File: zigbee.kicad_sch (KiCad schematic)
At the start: 59 parts, among them J201 Conn_Coaxial, J203 TC2050, U201 SKY13317-373, U202 CC2652P1FRGZR, U203 CC2652P1FRGZR, U204 CC2652PSIP, X201 32.768kHz, X202 48MHz

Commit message: Fixed SoC power circuitry
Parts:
- removed C201, C204, C206, C210: 1.5p, symbol Device:C
- removed C202, C221, C222, C223, C224, C225, C226: 0.1u, symbol Device:C
- removed C203, C219, C220: 22u, symbol Device:C
- removed C205: 0.5p, symbol Device:C
- removed C207, C211, C212, C216, C229: 12p, symbol Device:C
- removed C208: 15p, symbol Device:C
- removed C209: 1u, symbol Device:C
- removed C213, C214: 7.5p, symbol Device:C
- removed C215: 10n, symbol Device:C
- removed C217, C218, C227, C228: 1p, symbol Device:C
- removed C230: 470p, symbol Device:C
- removed D201: D_TVS, symbol Device:D_TVS
- removed J201: Conn_Coaxial, symbol Connector:Conn_Coaxial
- removed L201: 6.8u, symbol Device:L
- removed L202: 6.8n, symbol Device:L
- removed L203, L204: 2.4n, symbol Device:L
- removed L205: 3.3n, symbol Device:L
- removed L206: 2.7n, symbol Device:L
- removed L207: 20n, symbol Device:L
- removed L208, L209: 3.7n, symbol Device:L
- removed L210, L211: 3.4n, symbol Device:L
- removed R201: 100k, symbol Device:R
- removed R202, R207, R208: 0R, symbol Device:R
- removed U201: SKY13317-373, symbol SoftServicesSymbolLibrary:SKY13317-373
- removed U202, U203: CC2652P1FRGZR, symbol SoftServicesSymbolLibrary:CC2652P1FRGZR
- removed X201: 32.768kHz, symbol Device:Crystal
- removed X202: 48MHz, symbol Device:Crystal_GND24
- added C2001: 0.1u, symbol Device:C
- added C2002: 15p, symbol Device:C
- added J2002: Conn_Coaxial, symbol Connector:Conn_Coaxial
- added R2001: R, symbol Device:R
- U2001: renamed from U204; footprint (none) -> CC2652PSIP:CC2652PSIP
- renumbered FB201 to FB2001, J203 to J2001, R203 to R2002, R204 to R2003, R205 to R2004, R206 to R2005
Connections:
- net CC2652_LED1: now also U2001.24 (DIO6)
- net CC2652_LED2: now also U2001.25 (DIO7)
- net CC2652_RESET_N: now also U2001.4 (nRESET), C2001.1
- net CC2652_TCK: now also U2001.35 (TCK)
- net CC2652_TDI: now also U2001.37 (DIO17)
- net CC2652_TDO: now also U2001.36 (DIO16)
- net CC2652_TMS: now also U2001.34 (TMS)
- net CC2652_UART6_CTSn: now also R2005.2; no longer R2004.2
- net CC2652_UART6_RTSn: now also R2004.2; no longer R2005.2
- net CC2652_UART6_RXD: now also R2002.1; no longer R2003.1
- net CC2652_UART6_TXD: now also R2003.1; no longer R2002.1
- net GND: now also J2001.9, U2001.10 (GND), U2001.11 (GND), U2001.12 (GND), U2001.13 (GND), U2001.16 (GND), U2001.17 (GND), U2001.19 (GND), U2001.49 (GND), U2001.5 (GND), U2001.50 (GND), U2001.51 (GND), U2001.52 (GND), U2001.53 (GND), U2001.54 (GND), U2001.55 (GND), U2001.56 (GND), U2001.57 (GND), U2001.58 (GND), U2001.59 (GND), U2001.60 (GND), U2001.61 (GND), U2001.62 (GND), U2001.63 (GND), U2001.64 (GND), U2001.65 (GND), U2001.66 (GND), U2001.67 (GND), U2001.68 (GND), U2001.69 (GND), U2001.70 (GND), U2001.71 (GND), U2001.72 (GND), U2001.73 (GND), U2001.9 (GND), C2001.2, J2002.2 (Ext)
- net VDD3V3_CC: now also U2001.46 (VDDS), U2001.47 (VDDS_PU), R2001.2
- net VDD_3V3: now also R2001.1
- net at R2002.2: now also U2001.30 (DIO12)
- net at R2003.2: now also U2001.31 (DIO13)
- net at R2004.1: now also U2001.39 (DIO18)
- net at R2005.1: now also U2001.40 (DIO19)
- net at U2001.18 (RF): now also C2002.1
- new net: C2002.2, J2002.1 (In)
- no-connect marks 18 -> 2
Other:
- note added: "CC2652PSIP Zigbee Network"
- note removed: "CC2652P I/O Interface"
- note removed: "CC2652P Zigbee Network"
- note removed: "Decoupling Capacitors"
- note removed: "Need to configure GPIO for antenna to be connected to a path"
- moved on the sheet: FB2001, J2001, R2002, R2003, R2004, R2005, U2001

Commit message: Finished SoC schematic
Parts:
- removed R2001: R, symbol Device:R
- added D2001, D2002, D2003: D, symbol Device:D
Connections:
- net CC2652_RESET_N: now also D2001.2 (A), D2002.2 (A), D2003.2 (A)
- net CC2652_BOOT: now reaches U2001.33 (DIO15)
- new net CC2652_RSTn: D2001.1 (K)
- new net PORz_OUT: D2002.1 (K)
- new net RESETSTATz: D2003.1 (K)
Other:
- note added: "RB520S30T1G"

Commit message: Fixed ERC errors and warnings (zero errors and zero warnings)
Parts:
- renumbered R2002 to R2001, R2003 to R2002, R2004 to R2003, R2005 to R2004
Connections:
- no-connect marks 2 -> 25
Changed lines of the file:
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@@
+	)
+	(junction
+		(at 215.9 78.74)
+		(diameter 0)
+		(color 0 0 0 0)
 	)
 	(junction
@@
 	)
 	(no_connect
+		(at 133.35 129.54)
+	)
+	(no_connect
+		(at 133.35 111.76)
+	)
+	(no_connect
+		(at 133.35 167.64)
+	)
+	(no_connect
+		(at 133.35 172.72)
+	)
+	(no_connect
+		(at 133.35 109.22)
+	)
+	(no_connect
+		(at 133.35 175.26)
+	)
+	(no_connect
+		(at 133.35 182.88)
+	)
+	(no_connect
 		(at 300.99 95.25)
+	)
+	(no_connect
+		(at 133.35 116.84)
+	)
+	(no_connect
+		(at 133.35 132.08)
 	)
 	(no_connect
 		(at 133.35 96.52)
 	)
+	(no_connect
+		(at 133.35 157.48)
+	)
+	(no_connect
+		(at 133.35 165.1)
+	)
+	(no_connect
+		(at 133.35 160.02)
+	)
+	(no_connect
+		(at 133.35 127)
+	)
+	(no_connect
+		(at 133.35 185.42)
+	)
+	(no_connect
+		(at 133.35 177.8)
+	)
+	(no_connect
+		(at 133.35 162.56)
+	)
+	(no_connect
+		(at 133.35 180.34)
+	)
+	(no_connect
+		(at 133.35 142.24)
+	)
+	(no_connect
+		(at 133.35 134.62)
+	)
+	(no_connect
+		(at 133.35 114.3)
+	)
+	(no_connect
+		(at 133.35 106.68)
+	)
+	(no_connect
+		(at 133.35 170.18)
+	)
+	(no_connect
+		(at 133.35 119.38)
+	)
 	(wire
 		(pts
@@
 	(wire
 		(pts
-			(xy 217.17 73.66) (xy 217.17 78.74)
+			(xy 222.25 73.66) (xy 222.25 78.74)
 		)
 		(stroke
@@
 	(wire
 		(pts
-			(xy 210.82 78.74) (xy 217.17 78.74)
+			(xy 210.82 78.74) (xy 215.9 78.74)
 		)
 		(stroke
@@
 		(pts
 			(xy 100.33 114.3) (xy 100.33 116.84)
+		)
+		(stroke
+			(width 0)
+			(type default)
+		)
+	)
+	(wire
+		(pts
+			(xy 215.9 78.74) (xy 222.25 78.74)
 		)
 		(stroke
@@
 	)
 	(symbol
+		(lib_id "power:PWR_FLAG")
+		(at 215.9 78.74 0)
+		(unit 1)
+		(exclude_from_sim no)
+		(in_bom yes)
+		(on_board yes)
+		(dnp no)
+		(property "Reference" "#FLG04038"
+			(at 215.9 76.835 0)
+			(effects
+				(font
+					(size 1.27 1.27)
+				)
+				(hide yes)
+			)
+		)
+		(property "Value" "PWR_FLAG"
+			(at 215.9 74.422 0)
+			(effects
+				(font
+					(size 1.27 1.27)
+				)
+			)
+		)
+		(property "Footprint" ""
+			(at 215.9 78.74 0)
+			(effects
+				(font
+					(size 1.27 1.27)
+				)
+				(hide yes)
+			)
+		)
+		(property "Datasheet" "~"
+			(at 215.9 78.74 0)
+			(effects
+				(font
+					(size 1.27 1.27)
+				)
+				(hide yes)
+			)
+		)
+		(property "Description" "Special symbol for telling ERC where power comes from"
+			(at 215.9 78.74 0)
+			(effects
+				(font
+					(size 1.27 1.27)
+				)
+				(hide yes)
+			)
+		)
+		(pin "1"
+		)
+		(instances
+			(project "Leonhart"
+				(path "/b43b7bca-e50d-42ec-8ff0-e0016dfefe0a/4037e4ca-7763-453b-96d1-7d8342daaa99"
+					(reference "#FLG04038")
+					(unit 1)
+				)
+			)
+		)
+	)
+	(symbol
 		(lib_id "Device:C")
 		(at 148.59 101.6 90)
@@
 	(symbol
 		(lib_id "power:VDD")
-		(at 217.17 73.66 0)
+		(at 222.25 73.66 0)
 		(unit 1)
 		(exclude_from_sim no)
@@
 		(dnp no)
 		(property "Reference" "#PWR02002"
-			(at 217.17 77.47 0)
+			(at 222.25 77.47 0)
 			(effects
 				(font
@@
 		)
 		(property "Value" "VDD3V3_CC"
-			(at 212.852 68.58 0)
+			(at 217.932 68.58 0)
 			(effects
 				(font
@@
 		)
 		(property "Footprint" ""
-			(at 217.17 73.66 0)
+			(at 222.25 73.66 0)
 			(effects
 				(font
@@
 		)
 		(property "Datasheet" ""
-			(at 217.17 73.66 0)
+			(at 222.25 73.66 0)
 			(effects
 				(font
@@
 		)
 		(property "Description" "Power symbol creates a global label with name \"VDD\""
-			(at 217.17 73.66 0)
+			(at 222.25 73.66 0)
 			(effects
 				(font
@@
 		(on_board yes)
 		(dnp no)
-		(property "Reference" "R2005"
+		(property "Reference" "R2004"
 			(at 157.48 157.734 90)
 			(effects
@@
 			(project "Leonhart"
 				(path "/b43b7bca-e50d-42ec-8ff0-e0016dfefe0a/4037e4ca-7763-453b-96d1-7d8342daaa99"
-					(reference "R2005")
+					(reference "R2004")
 					(unit 1)
 				)
@@
 		(on_board yes)
 		(dnp no)
-		(property "Reference" "R2003"
+		(property "Reference" "R2002"
 			(at 157.48 142.494 90)
 			(effects
@@
 			(project "Leonhart"
 				(path "/b43b7bca-e50d-42ec-8ff0-e0016dfefe0a/4037e4ca-7763-453b-96d1-7d8342daaa99"
-					(reference "R2003")
+					(reference "R2002")
 					(unit 1)
 				)
@@
 		(on_board yes)
 		(dnp no)
-		(property "Reference" "R2004"
+		(property "Reference" "R2003"
 			(at 157.48 149.606 90)
 			(effects
@@
 			(project "Leonhart"
 				(path "/b43b7bca-e50d-42ec-8ff0-e0016dfefe0a/4037e4ca-7763-453b-96d1-7d8342daaa99"
-					(reference "R2004")
+					(reference "R2003")
 					(unit 1)
 				)
@@
 		(on_board yes)
 		(dnp no)
-		(property "Reference" "R2002"
+		(property "Reference" "R2001"
 			(at 157.48 134.62 90)
 			(effects
@@
 			(project ""
 				(path "/b43b7bca-e50d-42ec-8ff0-e0016dfefe0a/4037e4ca-7763-453b-96d1-7d8342daaa99"
-					(reference "R2002")
+					(reference "R2001")
 					(unit 1)
 				)

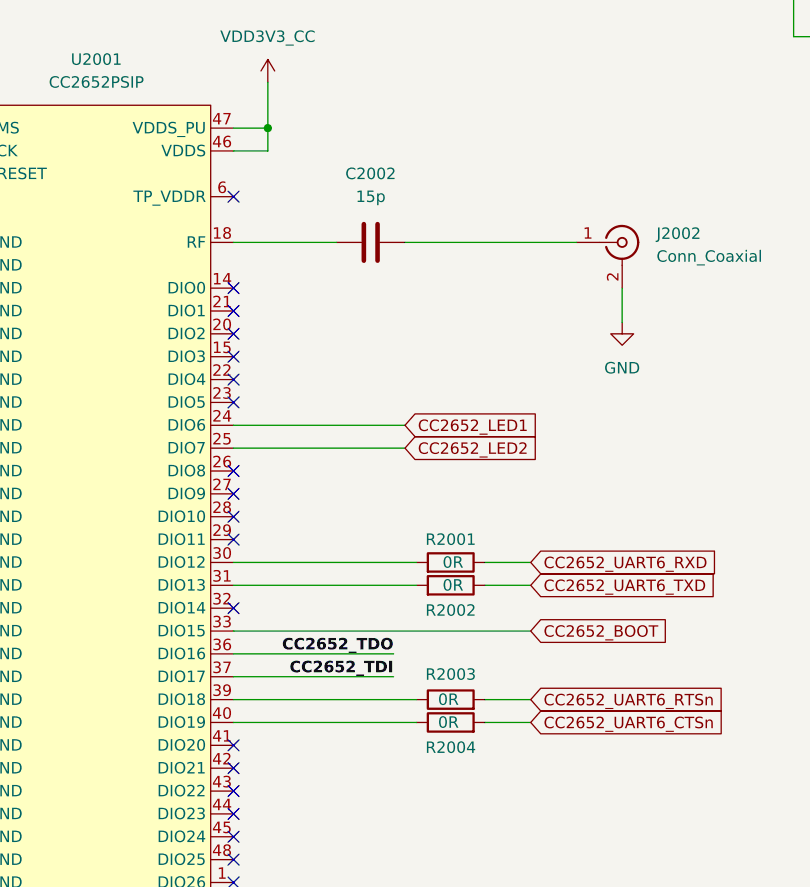
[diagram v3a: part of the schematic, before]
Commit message: Labeled all nets and added some footprints
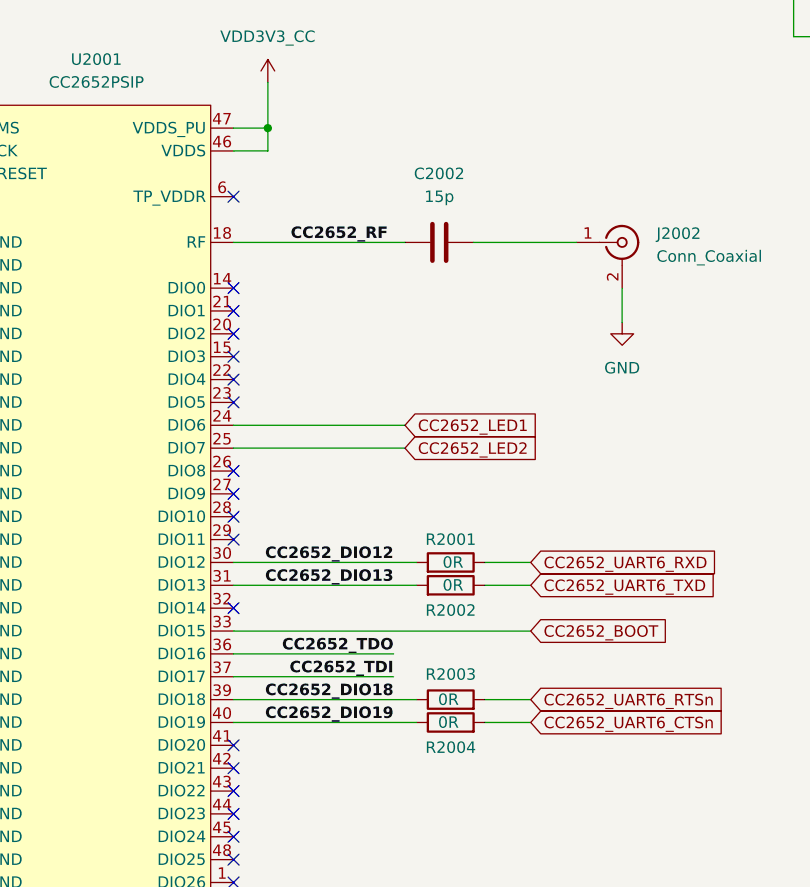
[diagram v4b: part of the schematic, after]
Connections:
- net CC2652_RF: now reaches C2002.1, U2001.18 (RF)
- net CC2652_DIO19: now reaches R2004.1, U2001.40 (DIO19)
- net CC2652_DIO13: now reaches R2002.2, U2001.31 (DIO13)
- net CC2652_DIO12: now reaches R2001.2, U2001.30 (DIO12)
- net CC2652_DIO18: now reaches R2003.1, U2001.39 (DIO18)
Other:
- moved on the sheet: C2002
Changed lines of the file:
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@@
 	(wire
 		(pts
-			(xy 133.35 101.6) (xy 144.78 101.6)
+			(xy 133.35 101.6) (xy 152.4 101.6)
 		)
 		(stroke
@@
 	(wire
 		(pts
-			(xy 152.4 101.6) (xy 171.45 101.6)
+			(xy 160.02 101.6) (xy 171.45 101.6)
 		)
 		(stroke
@@
 		)
 	)
+	(label "CC2652_DIO18"
+		(at 151.13 152.4 180)
+		(effects
+			(font
+				(size 1.27 1.27)
+				(thickness 0.254)
+				(bold yes)
+			)
+			(justify right bottom)
+		)
+	)
 	(label "CC2652_RESET_N"
 		(at 322.58 87.63 180)
@@
 		)
 	)
+	(label "CC2652_RF"
+		(at 139.7 101.6 0)
+		(effects
+			(font
+				(size 1.27 1.27)
+				(thickness 0.254)
+				(bold yes)
+			)
+			(justify left bottom)
+		)
+	)
+	(label "CC2652_DIO19"
+		(at 151.13 154.94 180)
+		(effects
+			(font
+				(size 1.27 1.27)
+				(thickness 0.254)
+				(bold yes)
+			)
+			(justify right bottom)
+		)
+	)
 	(label "CC2652_TDI"
 		(at 322.58 92.71 180)
@@
 		)
 	)
+	(label "CC2652_DIO12"
+		(at 151.13 137.16 180)
+		(effects
+			(font
+				(size 1.27 1.27)
+				(thickness 0.254)
+				(bold yes)
+			)
+			(justify right bottom)
+		)
+	)
 	(label "CC2652_TDI"
 		(at 151.13 149.86 180)
@@
 	(label "CC2652_RESET_N"
 		(at 217.17 189.23 180)
+		(effects
+			(font
+				(size 1.27 1.27)
+				(thickness 0.254)
+				(bold yes)
+			)
+			(justify right bottom)
+		)
+	)
+	(label "CC2652_DIO13"
+		(at 151.13 139.7 180)
 		(effects
 			(font
@@
 	(symbol
 		(lib_id "Device:C")
-		(at 148.59 101.6 90)
+		(at 156.21 101.6 90)
 		(unit 1)
 		(exclude_from_sim no)
@@
 		(fields_autoplaced yes)
 		(property "Reference" "C2002"
-			(at 148.59 93.98 90)
+			(at 156.21 93.98 90)
 			(effects
 				(font
@@
 		)
 		(property "Value" "15p"
-			(at 148.59 96.52 90)
+			(at 156.21 96.52 90)
 			(effects
 				(font
@@
 		)
 		(property "Footprint" ""
-			(at 152.4 100.6348 0)
+			(at 160.02 100.6348 0)
 			(effects
 				(font
@@
 		)
 		(property "Datasheet" "~"
-			(at 148.59 101.6 0)
+			(at 156.21 101.6 0)
 			(effects
 				(font
@@
 		)
 		(property "Description" "Unpolarized capacitor"
-			(at 148.59 101.6 0)
-			(effects
-				(font
+			(at 156.21 101.6 0)
+			(effects
+				(font

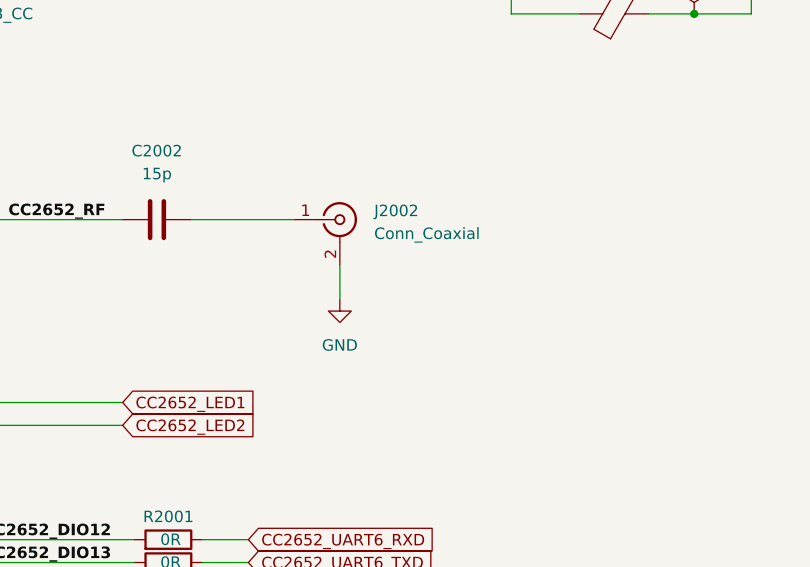
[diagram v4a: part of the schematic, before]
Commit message: Added many more footprints
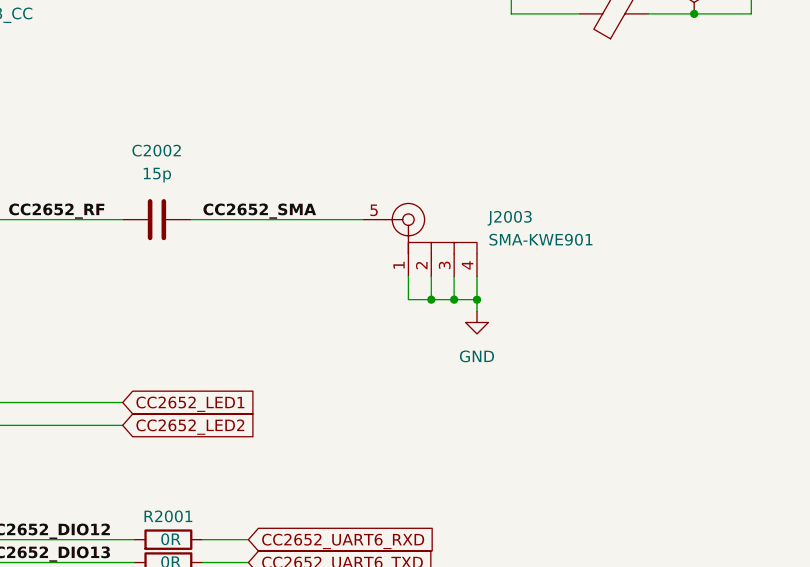
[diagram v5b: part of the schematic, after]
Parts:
- removed J2002: Conn_Coaxial, symbol Connector:Conn_Coaxial
- added J2003: SMA-KWE901, SoftServicesFootprintLibrary:SMA-KWE901, symbol SoftServicesSymbolLibrary:SMA-KWE901
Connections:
- net GND: now also J2003.1, J2003.2, J2003.3, J2003.4
- net CC2652_SMA: now reaches C2002.2
- net CC2652_SMA: now also J2003.5
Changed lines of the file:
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@@
+	)
+	(junction
+		(at 186.69 110.49)
+		(diameter 0)
+		(color 0 0 0 0)
 	)
 	(junction
@@
 	)
 	(junction
+		(at 191.77 110.49)
+		(diameter 0)
+		(color 0 0 0 0)
+	)
+	(junction
 		(at 100.33 119.38)
 		(diameter 0)
@@
 	(junction
 		(at 100.33 134.62)
+		(diameter 0)
+		(color 0 0 0 0)
+	)
+	(junction
+		(at 189.23 110.49)
 		(diameter 0)
 		(color 0 0 0 0)
@@
 	(wire
 		(pts
+			(xy 189.23 107.95) (xy 189.23 110.49)
+		)
+		(stroke
+			(width 0)
+			(type default)
+		)
+	)
+	(wire
+		(pts
 			(xy 100.33 147.32) (xy 100.33 149.86)
 		)
@@
 	(wire
 		(pts
+			(xy 186.69 110.49) (xy 184.15 110.49)
+		)
+		(stroke
+			(width 0)
+			(type default)
+		)
+	)
+	(wire
+		(pts
+			(xy 189.23 110.49) (xy 186.69 110.49)
+		)
+		(stroke
+			(width 0)
+			(type default)
+		)
+	)
+	(wire
+		(pts
 			(xy 100.33 149.86) (xy 102.87 149.86)
 		)
@@
 	(wire
 		(pts
+			(xy 186.69 107.95) (xy 186.69 110.49)
+		)
+		(stroke
+			(width 0)
+			(type default)
+		)
+	)
+	(wire
+		(pts
 			(xy 285.75 97.79) (xy 285.75 101.6)
 		)
@@
 	(wire
 		(pts
-			(xy 176.53 106.68) (xy 176.53 110.49)
+			(xy 184.15 107.95) (xy 184.15 110.49)
 		)
 		(stroke
@@
 	(wire
 		(pts
-			(xy 160.02 101.6) (xy 171.45 101.6)
+			(xy 160.02 101.6) (xy 179.07 101.6)
 		)
 		(stroke
@@
 	(wire
 		(pts
+			(xy 191.77 107.95) (xy 191.77 110.49)
+		)
+		(stroke
+			(width 0)
+			(type default)
+		)
+	)
+	(wire
+		(pts
 			(xy 100.33 177.8) (xy 102.87 177.8)
 		)
@@
 	(wire
 		(pts
+			(xy 191.77 110.49) (xy 189.23 110.49)
+		)
+		(stroke
+			(width 0)
+			(type default)
+		)
+	)
+	(wire
+		(pts
 			(xy 170.18 194.31) (xy 179.07 194.31)
 		)
@@
 		(pts
 			(xy 100.33 124.46) (xy 102.87 124.46)
+		)
+		(stroke
+			(width 0)
+			(type default)
+		)
+	)
+	(wire
+		(pts
+			(xy 191.77 110.49) (xy 191.77 111.76)
 		)
 		(stroke
@@
 	(label "CC2652_TMS"
 		(at 267.97 90.17 0)
+		(effects
+			(font
+				(size 1.27 1.27)
+				(thickness 0.254)
+				(bold yes)
+			)
+			(justify left bottom)
+		)
+	)
+	(label "CC2652_SMA"
+		(at 161.29 101.6 0)
 		(effects
 			(font
@@
 	(symbol
 		(lib_id "power:GND")
-		(at 176.53 110.49 0)
+		(at 191.77 111.76 0)
 		(unit 1)
 		(exclude_from_sim no)
@@
 		(fields_autoplaced yes)
 		(property "Reference" "#PWR02008"
-			(at 176.53 116.84 0)
+			(at 191.77 118.11 0)
 			(effects
 				(font
@@
 		)
 		(property "Value" "GND"
-			(at 176.53 115.57 0)
+			(at 191.77 116.84 0)
 			(effects
 				(font
@@
 		)
 		(property "Footprint" ""
-			(at 176.53 110.49 0)
+			(at 191.77 111.76 0)
 			(effects
 				(font
@@
 		)
 		(property "Datasheet" ""
-			(at 176.53 110.49 0)
+			(at 191.77 111.76 0)
 			(effects
 				(font
@@
 		)
 		(property "Description" "Power symbol creates a global label with name \"GND\" , ground"
-			(at 176.53 110.49 0)
+			(at 191.77 111.76 0)
 			(effects
 				(font
@@
 				(path "/b43b7bca-e50d-42ec-8ff0-e0016dfefe0a/4037e4ca-7763-453b-96d1-7d8342daaa99"
 					(reference "D2002")
+					(unit 1)
+				)
+			)
+		)
+	)
+	(symbol
+		(lib_id "SoftServicesSymbolLibrary:SMA-KWE901")
+		(at 184.15 101.6 0)
+		(unit 1)
+		(exclude_from_sim no)
+		(in_bom yes)
+		(on_board yes)
+		(dnp no)
+		(fields_autoplaced yes)
+		(property "Reference" "J2003"
+			(at 193.04 101.3368 0)
+			(effects
+				(font
+					(size 1.27 1.27)
+				)
+				(justify left)
+			)
+		)
+		(property "Value" "SMA-KWE901"
+			(at 193.04 103.8768 0)
+			(effects
+				(font
+					(size 1.27 1.27)
+				)
+				(justify left)
+			)
+		)
+		(property "Footprint" "SoftServicesFootprintLibrary:SMA-KWE901"
+			(at 184.15 101.6 0)
+			(effects
+				(font
+					(size 1.27 1.27)
+				)
+				(hide yes)
+			)
+		)
+		(property "Datasheet" ""
+			(at 184.15 101.6 0)
+			(effects
+				(font
+					(size 1.27 1.27)
+				)
+				(hide yes)
+			)
+		)
+		(property "Description" ""
+			(at 184.15 101.6 0)
+			(effects
+				(font
+					(size 1.27 1.27)
+				)
+				(hide yes)
+			)
+		)
+		(pin "2"
+		)
+		(pin "3"
+		)
+		(pin "5"
+		)
+		(pin "4"
+		)
+		(pin "1"
+		)
+		(instances
+			(project ""
+				(path "/b43b7bca-e50d-42ec-8ff0-e0016dfefe0a/4037e4ca-7763-453b-96d1-7d8342daaa99"
+					(reference "J2003")
 					(unit 1)
 				)
@@
 					(unit 1)
 				)
-			)
-		)
-	)
-	(symbol
-		(lib_id "Connector:Conn_Coaxial")
-		(at 176.53 101.6 0)
-		(unit 1)
-		(exclude_from_sim no)
-		(in_bom yes)
-		(on_board yes)
-		(dnp no)
-		(fields_autoplaced yes)
-		(property "Reference" "J2002"
-			(at 180.34 100.6231 0)
-			(effects
-				(font
-					(size 1.27 1.27)
-				)
-				(justify left)
-			)
-		)
-		(property "Value" "Conn_Coaxial"
-			(at 180.34 103.1631 0)
-			(effects
-				(font
-					(size 1.27 1.27)
-				)
-				(justify left)
-			)
-		)
-		(property "Footprint" ""
-			(at 176.53 101.6 0)
-			(effects
-				(font
-					(size 1.27 1.27)
-				)
-				(hide yes)
-			)
-		)
-		(property "Datasheet" "~"
-			(at 176.53 101.6 0)
-			(effects
-				(font
-					(size 1.27 1.27)
-				)
-				(hide yes)
-			)
-		)
-		(property "Description" "coaxial connector (BNC, SMA, SMB, SMC, Cinch/RCA, LEMO, ...)"
-			(at 176.53 101.6 0)
-			(effects
-				(font
-					(size 1.27 1.27)
-				)
-				(hide yes)
-			)
-		)
-		(pin "2"
-		)
-		(pin "1"
-		)
-		(instances
-			(project "Leonhart"
-				(path "/b43b7bca-e50d-42ec-8ff0-e0016dfefe0a/4037e4ca-7763-453b-96d1-7d8342daaa99"
-					(reference "J2002")
-					(unit 1)
-				)
